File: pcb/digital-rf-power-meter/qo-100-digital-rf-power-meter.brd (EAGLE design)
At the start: 60 x 30 mm, 14 parts, among them CON1 2EDG-5P, CON2 4P-SH-SIDE, U1 LTC4151HDD

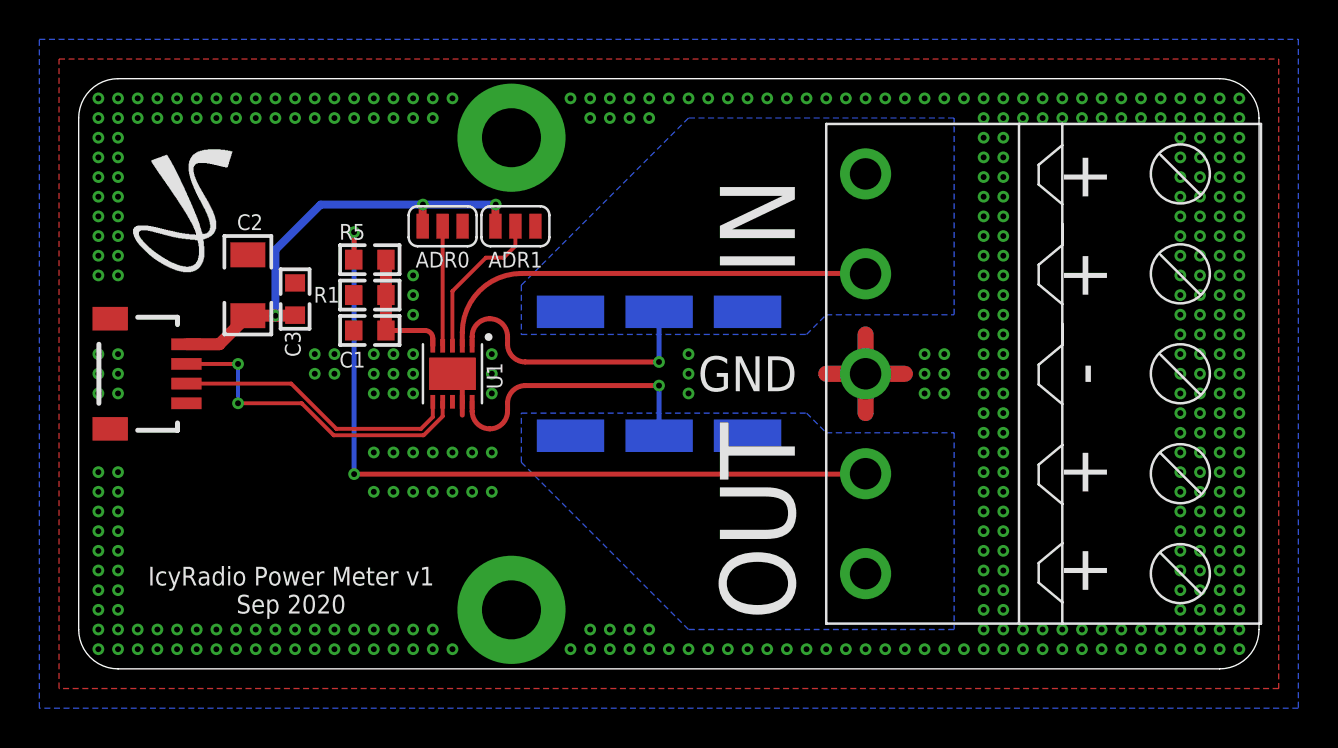
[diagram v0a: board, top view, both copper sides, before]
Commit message: Renamed RF Power meter Added Power meter Added IO expander to RF switch PCB to make it work thru I2C
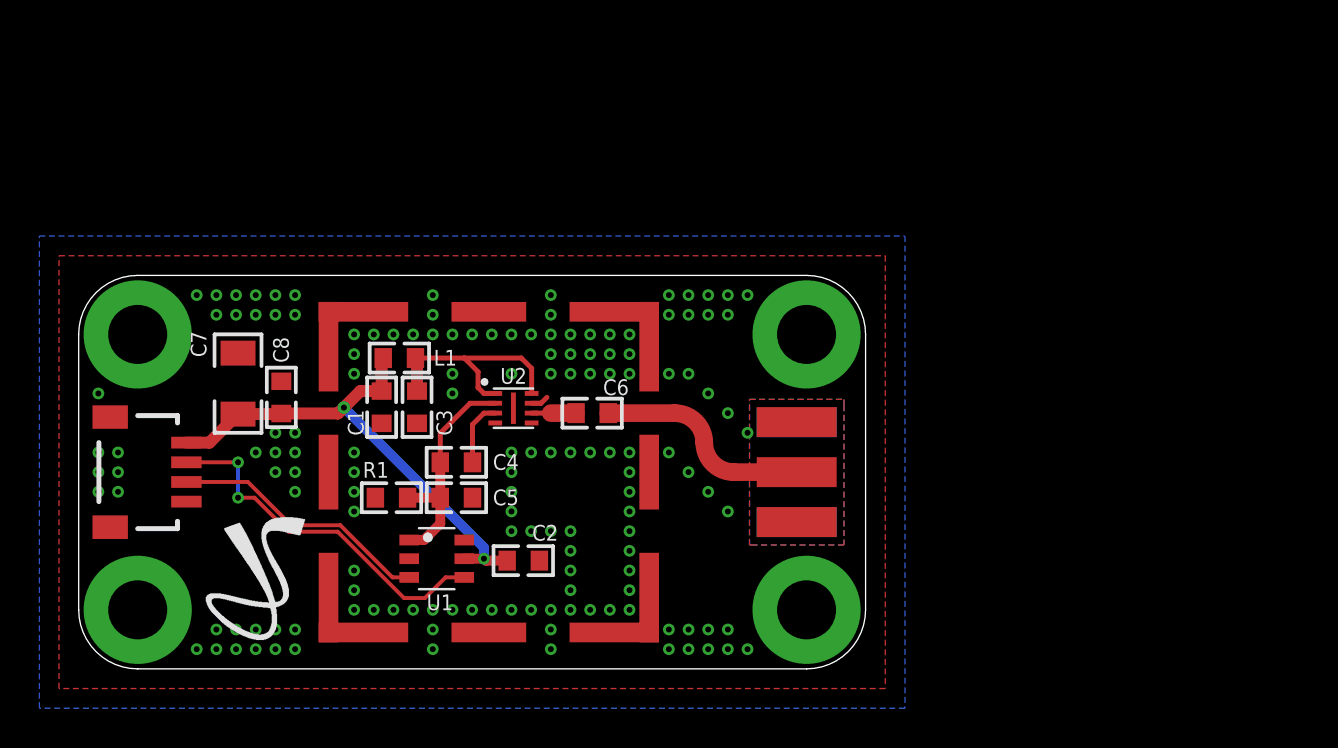
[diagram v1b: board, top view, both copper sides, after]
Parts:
- removed CON2: 4P-SH-SIDE, JST:SH-04-SIDE
- removed R2, R3, R4: 0.012 Ohms, Resistor:RES2512
- removed R5: 165K Ohms, Resistor:RES0603
- removed SJ1, SJ2: (no value), Solder Jumper:SJ2_S
- added C4, C5: DNP, Capacitor:CAP0603
- added C6, C8: 100nF, Capacitor:CAP0603
- added C7: 22uF, Capacitor:CAP1206
- added L1: 1.6uH, Inductor:IND0603
- added RFCON1: RFCON-SMA-EDGE, RF Connector:SMA-EDGE
- added SHIELD1: SHIELD-TE-2118707, Shield:2118707
- added U2: LTC5597, Analog Devices:DFN8_2X2
- C1: value 10nF -> 330pF
- C2: value 22uF -> 100nF; device Capacitor:CAP1206 -> Capacitor:CAP0603
- C3: value 100nF -> 330pF
- CON1: value 2EDG-5P -> 4P-SH-SIDE; device Generic Connector:2EDG-5P -> JST:SH-04-SIDE
- R1: value 10K Ohms -> DNP
- U1: value LTC4151HDD -> MCP3421-A0; device Analog Devices:DFN10 -> Microchip:SOT23-6
- moved CON1 37.8 mm to (2.50, 10.0), turned to 270 degrees
- moved C2 19.8 mm to (22.6, 5.50), turned to 0 degrees
- moved LOGO1 19.1 mm to (11.7, 7.90)
- moved R1 10.4 mm to (15.9, 8.70)
- moved U1 9.43 mm to (18.2, 5.60), turned to 0 degrees
- moved C3 8.29 mm to (17.2, 13.3), turned to 270 degrees
- moved C1 3.95 mm to (15.4, 13.3), turned to 270 degrees
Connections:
- removed net VIN: CON1.P$4, CON1.P$5, R2.2, R3.2, R4.2, U1.1, U1.2
- new net VPOWER_OUT: C4.1, C5.1, R1.2, U1.1, U2.2
- net 3V3: now also C1.1, C7.1, C8.1, CON1.1, L1.1, U1.5; no longer C3.1, CON2.1, SJ1.3, SJ2.3
- net GND: now also C5.2, C7.2, C8.2, CON1.4, RFCON1.GND@0, RFCON1.GND@1, RFCON1.GND@2, RFCON1.GND@3, SHIELD1.1, SHIELD1.10, SHIELD1.11, SHIELD1.12, SHIELD1.2, SHIELD1.3, SHIELD1.4, SHIELD1.5, SHIELD1.6, SHIELD1.7, SHIELD1.8, SHIELD1.9, U1.2, U1.6, U2.4, U2.5, U2.7, U2.9; no longer CON1.P$3, CON2.4, SJ1.1, SJ2.1, U1.11, U1.9
- net I2C_SCL: now also CON1.3, U1.3; no longer CON2.3, U1.6
- net I2C_SDA: now also CON1.2, U1.4; no longer CON2.2, U1.7
- net N$1: now also C6.1, U2.6; no longer C1.1, R1.2, R5.2, U1.5
- net N$2: now also C6.2, RFCON1.SIG; no longer CON1.P$1, CON1.P$2, R2.1, R3.1, R4.1, R5.1, U1.10
- net N$3: now also C4.2, U2.3; no longer SJ1.2, U1.4
- net N$4: now also C3.1, L1.2, U2.1, U2.8; no longer SJ2.2, U1.3
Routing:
- net N$2: track 53.8 -> 10.8 mm, vias 3 -> 0
- net VIN: track 36.5 -> 0.00 mm, vias 1 -> 0
- net GND: track 18.3 -> 0.90 mm, vias 412 -> 151
- net VPOWER_OUT: track 0.00 -> 11.6 mm
- net N$1: track 6.52 -> 2.26 mm
- net N$4: track 7.93 -> 11.9 mm
- net N$3: track 6.07 -> 3.32 mm
- net 3V3: track 23.9 -> 25.6 mm, vias 3 -> 2
- net I2C_SDA: track 16.8 -> 18.5 mm
- net I2C_SCL: track 14.5 -> 13.3 mm
- removed copper zone on layer 16, net N$2
- removed copper zone on layer 16, net VIN
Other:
- board size 60 x 30 mm -> 40 x 20 mm
- board text added: "IcyRadio RF Power Meter v1 Sep 2020"
- board text removed: "+"
- board text removed: "-"
- board text removed: "ADR0"
- board text removed: "ADR1"
- board text removed: "GND"
- board text removed: "IN"
- board text removed: "IcyRadio Power Meter v1 Sep 2020"
- board text removed: "OUT"

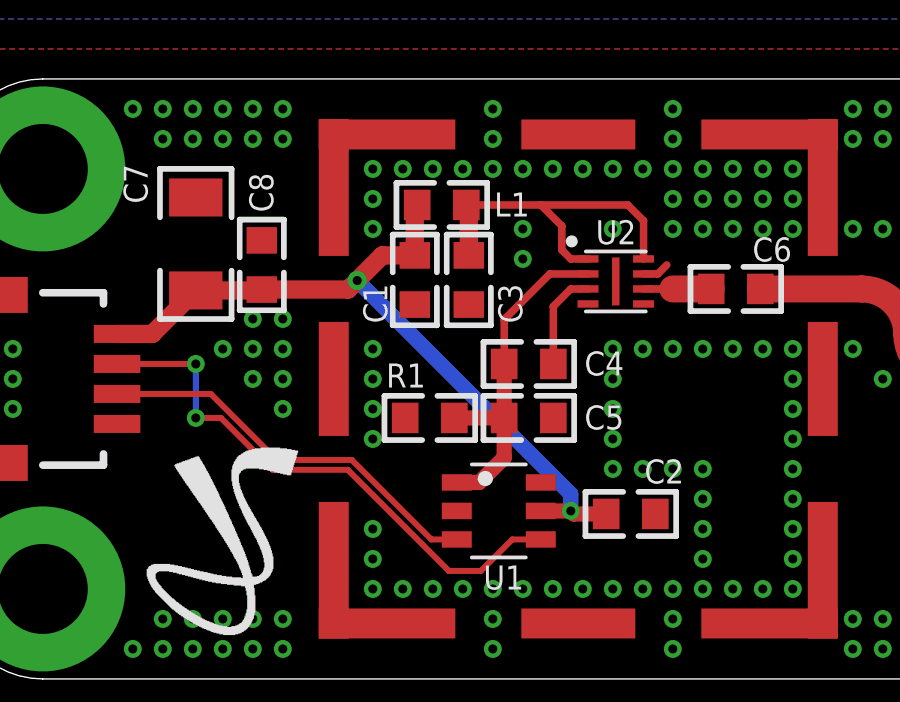
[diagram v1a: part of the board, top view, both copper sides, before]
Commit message: Add Ripple blocker to RF power meter
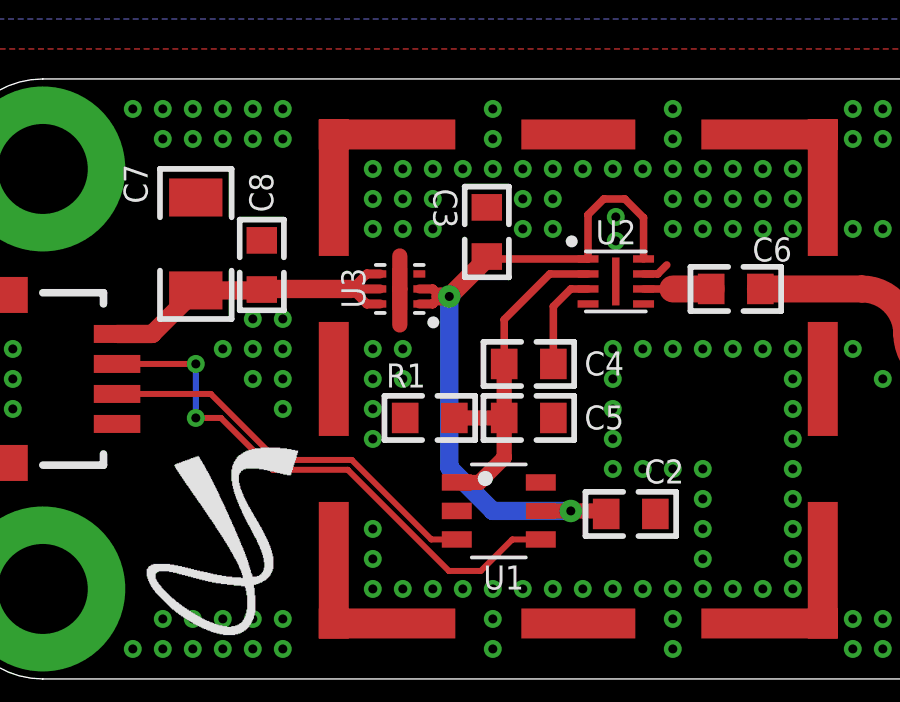
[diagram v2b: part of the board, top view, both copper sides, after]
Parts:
- removed C1: 330pF, Capacitor:CAP0603
- removed L1: 1.6uH, Inductor:IND0603
- added U3: MIC94305, Microchip:DFN6
- C2: value 100nF -> 4.7uF
- C3: value 330pF -> 4.7uF
- moved C3 1.71 mm to (17.8, 14.9), turned to 90 degrees
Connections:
- removed net N$4: C3.1, L1.2, U2.1, U2.8
- new net 3V3_CLEAN: C2.1, C3.1, U1.5, U2.1, U2.8, U3.1, U3.2
- net 3V3: now also U3.4, U3.5, U3.6; no longer C1.1, C2.1, L1.1, U1.5
- net GND: now also U3.3, U3.7; no longer C1.2
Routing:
- net 3V3_CLEAN: track 0.00 -> 24.9 mm, vias 0 -> 2
- net 3V3: track 25.6 -> 11.7 mm, vias 2 -> 0
- net N$4: track 11.9 -> 0.00 mm
- net GND: track 0.90 -> 3.20 mm, vias 151 -> 160

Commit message: Work on PCBs
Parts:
- C4: value DNP -> 10nF
- C5: value DNP -> 1uF
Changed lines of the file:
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@@
 <drawing>
 <settings>
-<setting alwaysvectorfont="yes"/>
+<setting alwaysvectorfont="no"/>
 <setting verticaltext="up"/>
 </settings>
@@
 <attribute name="VOLTAGE" value="" x="17.8" y="14.9" size="0.8" layer="27" font="vector" ratio="10" rot="R90" display="off"/>
 </element>
-<element name="C4" library="Capacitor" package="CAP0603" value="DNP" x="19.2" y="10.5" smashed="yes">
+<element name="C4" library="Capacitor" package="CAP0603" value="10nF" x="19.2" y="10.5" smashed="yes">
 <attribute name="NAME" x="21.0536" y="10.516" size="0.8" layer="25" font="vector" ratio="10" rot="SR0" align="center-left"/>
 <attribute name="VALUE" x="16.2536" y="8.468" size="0.8" layer="27" font="vector" ratio="10" rot="SR0" align="center-left"/>
 <attribute name="VOLTAGE" value="" x="19.2" y="10.5" size="0.8" layer="27" font="vector" ratio="10" display="off"/>
 </element>
-<element name="C5" library="Capacitor" package="CAP0603" value="DNP" x="19.2" y="8.7" smashed="yes">
+<element name="C5" library="Capacitor" package="CAP0603" value="1uF" x="19.2" y="8.7" smashed="yes">
 <attribute name="NAME" x="21.0536" y="8.716" size="0.8" layer="25" font="vector" ratio="10" rot="SR0" align="center-left"/>
 <attribute name="VALUE" x="16.2536" y="6.668" size="0.8" layer="27" font="vector" ratio="10" rot="SR0" align="center-left"/>
